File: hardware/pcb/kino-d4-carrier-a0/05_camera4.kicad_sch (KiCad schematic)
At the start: 20 parts, among them J500 XIAO ESP32-S3 Sense socket, J501 GPIO breakout - SD/strap rest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, U500 TXU0304PWR, U501 TPS2553DBVR

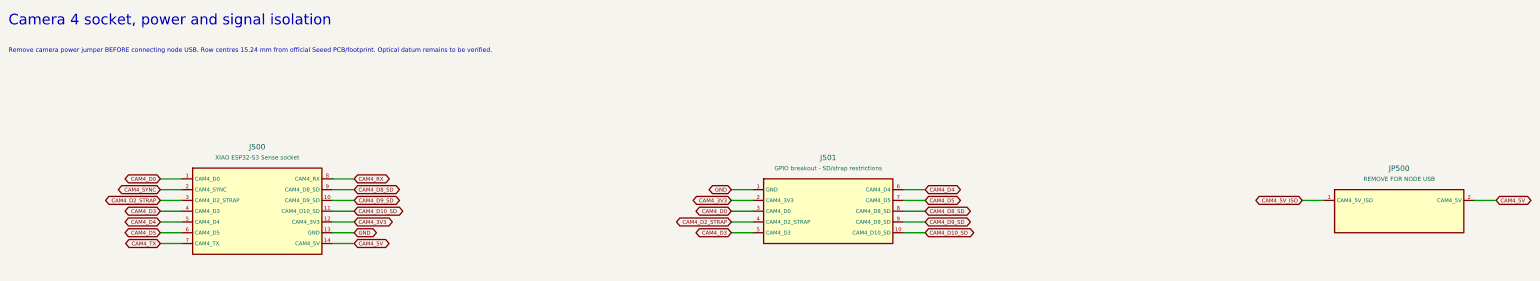
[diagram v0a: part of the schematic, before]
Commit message: feat(hardware): carrier A0.2 - external connections to the back, 0 ohm power links
- Cable connectors (J102, J601, J800, J900-J904, J1300), the camera GPIO
  breakout headers J201-J501, J101 and the P4 ribbon J100 move to B.Cu so
  the socketed XIAOs are the tallest parts on the front (MECHANICAL.md,
  face assignment). Pogo/sense contacts stay on the front.
- JP200-JP500 and JP1200 become Vishay CRCW12060000Z0EAHP 0 ohm links
  (10 A, <=5 mOhm) on a project land drawn from the Vishay reflow pads;
  capture, BOM, ERC and netlist regenerated.
- P4_5V_ISO feed re-run on In2 at 2.0 mm with 3-via layer changes.
- Connector labels follow their connectors to B.SilkS.
- 195 connections are open again after the move; DRC has no clearance,
  short, courtyard or silk errors (dangling lane ends only).

Co-Authored-By: Claude Opus 5.5 <noreply@anthropic.com>
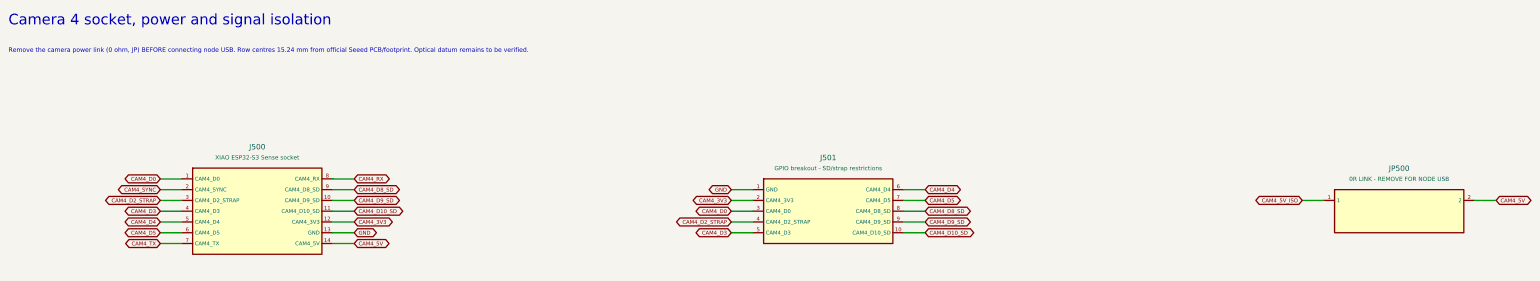
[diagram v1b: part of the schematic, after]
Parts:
- D500: Design note Reverse node USB-to-carrier isolation; does not prevent carrier-to-host VBUS feed without removing jumper. -> Reverse node USB-to-carrier isolation; does not prevent carrier-to-host VBUS feed without removing the link.
- J500: Design note Two 1x07 sockets; 22 mm camera pitch. 5V shared with node USB; isolate via jumper for USB service. -> Two 1x07 sockets; 22 mm camera pitch. 5V shared with node USB; isolate via the 0 ohm link for USB service.
- JP500: value REMOVE FOR NODE USB -> 0R LINK - REMOVE FOR NODE USB; footprint Connector_PinHeader_2.54mm:PinHeader_1x02_P2.54mm_Vertical -> KINO_A0:R_1206_3216Metric_Vishay_CRCW-HP; Design note Fit removable shunt during camera operation, remove before 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 -> 0 ohm link, fitted for camera operation. Desolder before co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
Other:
- note added: "Remove the camera power link (0 ohm, JP) BEFORE connecting node USB. Row centres 15.24 mm from official Seeed PCB/footprint. Optical datum remains to be verified."
- note removed: "Remove camera power jumper BEFORE connecting node USB. Row centres 15.24 mm from official Seeed PCB/footprint. Optical datum remains to be verified."
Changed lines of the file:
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@@
       (company "KINO") (comment 1 "ENGINEERING DRAFT - NOT FOR FABRICATION"))
 (text "Camera 4 socket, power and signal isolation" (at 15 12 0) (effects (font (size 2.5 2.5)) (justify left top)))
-(text "Remove camera power jumper BEFORE connecting node USB. Row centres 15.24 mm from official Seeed PCB/footprint. Optical datum remains to be verified." (at 15 20 0) (effects (font (size 1.05 1.05)) (justify left top)))
+(text "Remove the camera power link (0 ohm, JP) BEFORE connecting node USB. Row centres 15.24 mm from official Seeed PCB/footprint. Optical datum remains to be verified." (at 15 20 0) (effects (font (size 1.05 1.05)) (justify left top)))
 (symbol (lib_id "KINO_A0:J500") (at 73.66 58.42 0) (unit 1)
                   (in_bom yes) (on_board yes) (dnp no)
@@
                   (property "Footprint" "KINO_A0:XIAO_Socket_15.24mm" (at 73.66 58.42 0) (effects (font (size 1 1)) (hide yes)))
                   (property "Datasheet" "https://www.we-online.com/components/products/datasheet/61300711821.pdf" (at 73.66 58.42 0) (effects (font (size 1 1)) (hide yes)))
-                  (property "Design note" "Two 1x07 sockets; 22 mm camera pitch. 5V shared with node USB; isolate via jumper for USB service." (at 73.66 58.42 0) (effects (font (size 1 1)) (hide yes)))
+                  (property "Design note" "Two 1x07 sockets; 22 mm camera pitch. 5V shared with node USB; isolate via the 0 ohm link for USB service." (at 73.66 58.42 0) (effects (font (size 1 1)) (hide yes)))
                   (pin "1")(pin "2")(pin "3")(pin "4")(pin "5")(pin "6")(pin "7")(pin "8")(pin "9")(pin "10")(pin "11")(pin "12")(pin "13")(pin "14")
                   (instances (project "KINO_D4_Carrier_A0" (path "/3e6ce248-02da-5043-9ed8-b7ca2a49de29/98c561ab-7625-5940-bd5e-29e85052e268" (reference "J500") (unit 1)))))
@@
                   (in_bom yes) (on_board yes) (dnp no)
                   (property "Reference" "JP500" (at 342.9 48.34 0) (effects (font (size 1.27 1.27))))
-                  (property "Value" "REMOVE FOR NODE USB" (at 342.9 50.84 0) (effects (font (size 1.0 1.0))))
-                  (property "Footprint" "Connector_PinHeader_2.54mm:PinHeader_1x02_P2.54mm_Vertical" (at 342.9 58.42 0) (effects (font (size 1 1)) (hide yes)))
-                  (property "Datasheet" "https://www.we-online.com/components/products/datasheet/61300211121.pdf ; https://www.we-online.com/components/products/datasheet/60900213421.pdf" (at 342.9 58.42 0) (effects (font (size 1 1)) (hide yes)))
-                  (property "Design note" "Fit removable shunt during camera operation, remove before USB cable insertion." (at 342.9 58.42 0) (effects (font (size 1 1)) (hide yes)))
+                  (property "Value" "0R LINK - REMOVE FOR NODE USB" (at 342.9 50.84 0) (effects (font (size 1.0 1.0))))
+                  (property "Footprint" "KINO_A0:R_1206_3216Metric_Vishay_CRCW-HP" (at 342.9 58.42 0) (effects (font (size 1 1)) (hide yes)))
+                  (property "Datasheet" "https://www.vishay.com/docs/20043/crcwhpe3.pdf" (at 342.9 58.42 0) (effects (font (size 1 1)) (hide yes)))
+                  (property "Design note" "0 ohm link, fitted for camera operation. Desolder before connecting node USB; refit after. Flat on the front: the XIAO stays the tallest part there." (at 342.9 58.42 0) (effects (font (size 1 1)) (hide yes)))
                   (pin "1")(pin "2")
                   (instances (project "KINO_D4_Carrier_A0" (path "/3e6ce248-02da-5043-9ed8-b7ca2a49de29/98c561ab-7625-5940-bd5e-29e85052e268" (reference "JP500") (unit 1)))))
@@
                   (property "Footprint" "Diode_SMD:D_SMA" (at 342.9 167.64000000000001 0) (effects (font (size 1 1)) (hide yes)))
                   (property "Datasheet" "https://www.diodes.com/datasheet/download/B340A.pdf" (at 342.9 167.64000000000001 0) (effects (font (size 1 1)) (hide yes)))
-                  (property "Design note" "Reverse node USB-to-carrier isolation; does not prevent carrier-to-host VBUS feed without removing jumper." (at 342.9 167.64000000000001 0) (effects (font (size 1 1)) (hide yes)))
+                  (property "Design note" "Reverse node USB-to-carrier isolation; does not prevent carrier-to-host VBUS feed without removing the link." (at 342.9 167.64000000000001 0) (effects (font (size 1 1)) (hide yes)))
                   (pin "1")(pin "2")
                   (instances (project "KINO_D4_Carrier_A0" (path "/3e6ce248-02da-5043-9ed8-b7ca2a49de29/98c561ab-7625-5940-bd5e-29e85052e268" (reference "D500") (unit 1)))))

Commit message: feat(hardware): carrier A0.2 release pass - ready for fabrication with manual checks
Release review of the routed A0.2 carrier (A02-RELEASE.md: release matrix,
manual checks before ordering, bring-up tests). Final status: READY FOR
FABRICATION WITH SPECIFIC MANUAL CHECKS.

- USB-C input survives an unprogrammed STUSB4500 (20 V): D1001 SMF22A,
  R1004 10k, PD and load-switch P-FETs AO4409.
- Boost enable: R1204 100k BOOST_ENABLE to SYS_RAW (LTC2955-1 EN is a 2 uA
  source), Q1202 PMV16UN.
- I2C buffer U100 sides swapped (local bus on the TCA9517 A side's hard
  low); R100/R101 2.2k/22k hold EN low with JP1 pin 1 open.
- R105 SYNC_MASTER pull-down; D903 ESD on FN_N; TP1001 removed.
- SYS_RAW battery path as B.Cu and In2 pours with 25 extra vias; 1 oz inner
  copper in the stackup.
- XIAO socket pads get their solder-mask openings (footprint generator bug).
- Three fiducials per face; vias out of and away from pads; U1200 outline and
  pin-1 mark; legend lines and strokes 0.15 mm; silk association pass;
  CARRIER A0.2 / 2026-10 / S/N marking.
- Fab package (fab_a02.py): Gerbers + job file, drill, zip, placement files,
  fab BOM matched to LCSC by part number, hand-fit socket list, fab notes.
- Firmware constants header kino_carrier_a02.h.

DRC 0 / unconnected 0, ERC 0, verify.py --a02 passes.

Co-Authored-By: Claude Opus 5.5 <noreply@anthropic.com>
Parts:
- C500, C501, C504: value 100n 16V -> 100n 50V
- C502: value 1u 16V -> 1u 50V
- RS500: value 0.020 1% 0.5W -> 0.020 1% 1W; Design note Kelvin sense required; exact current-sense resistor MPN pen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 -> Kelvin pair to U700 from the pad inner corners (route_a02_k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
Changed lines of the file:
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@@
                   (in_bom yes) (on_board yes) (dnp no)
                   (property "Reference" "C500" (at 477.52 83.9 0) (effects (font (size 1.27 1.27))))
-                  (property "Value" "100n 16V" (at 477.52 86.4 0) (effects (font (size 1.0 1.0))))
+                  (property "Value" "100n 50V" (at 477.52 86.4 0) (effects (font (size 1.0 1.0))))
                   (property "Footprint" "Capacitor_SMD:C_0603_1608Metric" (at 477.52 96.52000000000001 0) (effects (font (size 1 1)) (hide yes)))
                   (property "Datasheet" "https://www.yageogroup.com/component-documentation/download/specsheet/CC0603KRX7R9BB104" (at 477.52 96.52000000000001 0) (effects (font (size 1 1)) (hide yes)))
@@
                   (in_bom yes) (on_board yes) (dnp no)
                   (property "Reference" "C501" (at 73.66 119.45999999999998 0) (effects (font (size 1.27 1.27))))
-                  (property "Value" "100n 16V" (at 73.66 121.95999999999998 0) (effects (font (size 1.0 1.0))))
+                  (property "Value" "100n 50V" (at 73.66 121.95999999999998 0) (effects (font (size 1.0 1.0))))
                   (property "Footprint" "Capacitor_SMD:C_0603_1608Metric" (at 73.66 132.07999999999998 0) (effects (font (size 1 1)) (hide yes)))
                   (property "Datasheet" "https://www.yageogroup.com/component-documentation/download/specsheet/CC0603KRX7R9BB104" (at 73.66 132.07999999999998 0) (effects (font (size 1 1)) (hide yes)))
@@
                   (in_bom yes) (on_board yes) (dnp no)
                   (property "Reference" "RS500" (at 208.28 155.02 0) (effects (font (size 1.27 1.27))))
-                  (property "Value" "0.020 1% 0.5W" (at 208.28 157.52 0) (effects (font (size 1.0 1.0))))
+                  (property "Value" "0.020 1% 1W" (at 208.28 157.52 0) (effects (font (size 1.0 1.0))))
                   (property "Footprint" "Resistor_SMD:R_1206_3216Metric" (at 208.28 167.64000000000001 0) (effects (font (size 1 1)) (hide yes)))
                   (property "Datasheet" "https://www.vishay.com/docs/30122/wslp.pdf" (at 208.28 167.64000000000001 0) (effects (font (size 1 1)) (hide yes)))
-                  (property "Design note" "Kelvin sense required; exact current-sense resistor MPN pending." (at 208.28 167.64000000000001 0) (effects (font (size 1 1)) (hide yes)))
+                  (property "Design note" "Kelvin pair to U700 from the pad inner corners (route_a02_kelvin.py)." (at 208.28 167.64000000000001 0) (effects (font (size 1 1)) (hide yes)))
                   (pin "1")(pin "2")
                   (instances (project "KINO_D4_Carrier_A0" (path "/3e6ce248-02da-5043-9ed8-b7ca2a49de29/98c561ab-7625-5940-bd5e-29e85052e268" (reference "RS500") (unit 1)))))
@@
                   (in_bom yes) (on_board yes) (dnp no)
                   (property "Reference" "C502" (at 477.52 155.02 0) (effects (font (size 1.27 1.27))))
-                  (property "Value" "1u 16V" (at 477.52 157.52 0) (effects (font (size 1.0 1.0))))
+                  (property "Value" "1u 50V" (at 477.52 157.52 0) (effects (font (size 1.0 1.0))))
                   (property "Footprint" "Capacitor_SMD:C_0603_1608Metric" (at 477.52 167.64000000000001 0) (effects (font (size 1 1)) (hide yes)))
                   (property "Datasheet" "https://weblib.samsungsem.com/mlcc/mlcc-ec-data-sheet.do?partNumber=CL10A105KB8NNN" (at 477.52 167.64000000000001 0) (effects (font (size 1 1)) (hide yes)))
@@
                   (in_bom yes) (on_board yes) (dnp no)
                   (property "Reference" "C504" (at 208.28 190.58 0) (effects (font (size 1.27 1.27))))
-                  (property "Value" "100n 16V" (at 208.28 193.08 0) (effects (font (size 1.0 1.0))))
+                  (property "Value" "100n 50V" (at 208.28 193.08 0) (effects (font (size 1.0 1.0))))
                   (property "Footprint" "Capacitor_SMD:C_0603_1608Metric" (at 208.28 203.20000000000002 0) (effects (font (size 1 1)) (hide yes)))
                   (property "Datasheet" "https://www.yageogroup.com/component-documentation/download/specsheet/CC0603KRX7R9BB104" (at 208.28 203.20000000000002 0) (effects (font (size 1 1)) (hide yes)))
